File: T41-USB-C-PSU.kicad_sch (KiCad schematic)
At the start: 2 parts

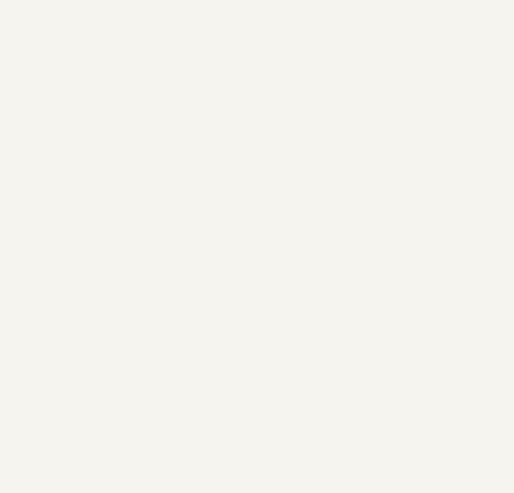
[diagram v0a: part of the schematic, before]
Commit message: Add tooling holes
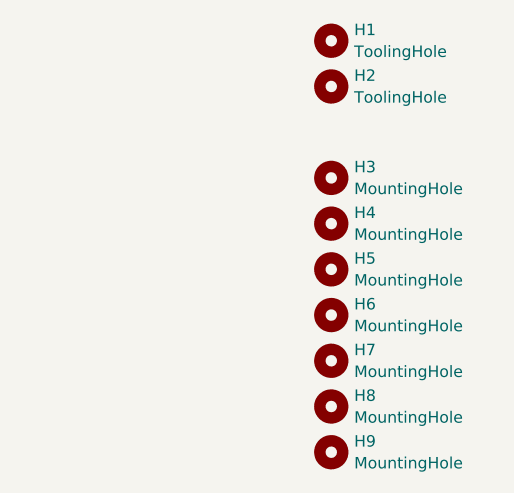
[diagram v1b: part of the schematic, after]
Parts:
- added H1, H2: ToolingHole, ToolingHole:ToolingHole_JLCSMT, symbol Mechanical:MountingHole
- added H3, H4, H5, H6, H7, H8, H9: MountingHole, MountingHole:MountingHole_2.2mm_M2, symbol Mechanical:MountingHole
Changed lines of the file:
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@@
     (stroke (width 0) (type default))
+  )
+  (symbol (lib_id "Mechanical:MountingHole") (at 267.97 35.56 0) (unit 1)
+    (in_bom no) (on_board yes) (dnp no) (fields_autoplaced)
+    (property "Reference" "H4" (at 270.51 34.3479 0)
+      (effects (font (size 1.27 1.27)) (justify left))
+    )
+    (property "Value" "MountingHole" (at 270.51 36.7721 0)
+      (effects (font (size 1.27 1.27)) (justify left))
+    )
+    (property "Footprint" "MountingHole:MountingHole_2.2mm_M2" (at 267.97 35.56 0)
+      (effects (font (size 1.27 1.27)) hide)
+    )
+    (property "Datasheet" "~" (at 267.97 35.56 0)
+      (effects (font (size 1.27 1.27)) hide)
+    )
+    (instances
+      (project "T41-USB-C-PSU"
+        (path "/4326e964-0a41-4fb3-bb68-131ba9c4f396"
+          (reference "H4") (unit 1)
+        )
+      )
+    )
+  )
+  (symbol (lib_id "Mechanical:MountingHole") (at 267.97 45.72 0) (unit 1)
+    (in_bom no) (on_board yes) (dnp no) (fields_autoplaced)
+    (property "Reference" "H6" (at 270.51 44.5079 0)
+      (effects (font (size 1.27 1.27)) (justify left))
+    )
+    (property "Value" "MountingHole" (at 270.51 46.9321 0)
+      (effects (font (size 1.27 1.27)) (justify left))
+    )
+    (property "Footprint" "MountingHole:MountingHole_2.2mm_M2" (at 267.97 45.72 0)
+      (effects (font (size 1.27 1.27)) hide)
+    )
+    (property "Datasheet" "~" (at 267.97 45.72 0)
+      (effects (font (size 1.27 1.27)) hide)
+    )
+    (instances
+      (project "T41-USB-C-PSU"
+        (path "/4326e964-0a41-4fb3-bb68-131ba9c4f396"
+          (reference "H6") (unit 1)
+        )
+      )
+    )
+  )
+  (symbol (lib_id "Mechanical:MountingHole") (at 267.97 50.8 0) (unit 1)
+    (in_bom no) (on_board yes) (dnp no) (fields_autoplaced)
+    (property "Reference" "H7" (at 270.51 49.5879 0)
+      (effects (font (size 1.27 1.27)) (justify left))
+    )
+    (property "Value" "MountingHole" (at 270.51 52.0121 0)
+      (effects (font (size 1.27 1.27)) (justify left))
+    )
+    (property "Footprint" "MountingHole:MountingHole_2.2mm_M2" (at 267.97 50.8 0)
+      (effects (font (size 1.27 1.27)) hide)
+    )
+    (property "Datasheet" "~" (at 267.97 50.8 0)
+      (effects (font (size 1.27 1.27)) hide)
+    )
+    (instances
+      (project "T41-USB-C-PSU"
+        (path "/4326e964-0a41-4fb3-bb68-131ba9c4f396"
+          (reference "H7") (unit 1)
+        )
+      )
+    )
+  )
+  (symbol (lib_id "Mechanical:MountingHole") (at 267.97 40.64 0) (unit 1)
+    (in_bom no) (on_board yes) (dnp no) (fields_autoplaced)
+    (property "Reference" "H5" (at 270.51 39.4279 0)
+      (effects (font (size 1.27 1.27)) (justify left))
+    )
+    (property "Value" "MountingHole" (at 270.51 41.8521 0)
+      (effects (font (size 1.27 1.27)) (justify left))
+    )
+    (property "Footprint" "MountingHole:MountingHole_2.2mm_M2" (at 267.97 40.64 0)
+      (effects (font (size 1.27 1.27)) hide)
+    )
+    (property "Datasheet" "~" (at 267.97 40.64 0)
+      (effects (font (size 1.27 1.27)) hide)
+    )
+    (instances
+      (project "T41-USB-C-PSU"
+        (path "/4326e964-0a41-4fb3-bb68-131ba9c4f396"
+          (reference "H5") (unit 1)
+        )
+      )
+    )
+  )
+  (symbol (lib_id "Mechanical:MountingHole") (at 267.97 15.24 0) (unit 1)
+    (in_bom no) (on_board yes) (dnp no) (fields_autoplaced)
+    (property "Reference" "H1" (at 270.51 14.0279 0)
+      (effects (font (size 1.27 1.27)) (justify left))
+    )
+    (property "Value" "ToolingHole" (at 270.51 16.4521 0)
+      (effects (font (size 1.27 1.27)) (justify left))
+    )
+    (property "Footprint" "ToolingHole:ToolingHole_JLCSMT" (at 267.97 15.24 0)
+      (effects (font (size 1.27 1.27)) hide)
+    )
+    (property "Datasheet" "~" (at 267.97 15.24 0)
+      (effects (font (size 1.27 1.27)) hide)
+    )
+    (instances
+      (project "T41-USB-C-PSU"
+        (path "/4326e964-0a41-4fb3-bb68-131ba9c4f396"
+          (reference "H1") (unit 1)
+        )
+      )
+    )
+  )
+  (symbol (lib_id "Mechanical:MountingHole") (at 267.97 60.96 0) (unit 1)
+    (in_bom no) (on_board yes) (dnp no) (fields_autoplaced)
+    (property "Reference" "H9" (at 270.51 59.7479 0)
+      (effects (font (size 1.27 1.27)) (justify left))
+    )
+    (property "Value" "MountingHole" (at 270.51 62.1721 0)
+      (effects (font (size 1.27 1.27)) (justify left))
+    )
+    (property "Footprint" "MountingHole:MountingHole_2.2mm_M2" (at 267.97 60.96 0)
+      (effects (font (size 1.27 1.27)) hide)
+    )
+    (property "Datasheet" "~" (at 267.97 60.96 0)
+      (effects (font (size 1.27 1.27)) hide)
+    )
+    (instances
+      (project "T41-USB-C-PSU"
+        (path "/4326e964-0a41-4fb3-bb68-131ba9c4f396"
+          (reference "H9") (unit 1)
+        )
+      )
+    )
+  )
+  (symbol (lib_id "Mechanical:MountingHole") (at 267.97 30.48 0) (unit 1)
+    (in_bom no) (on_board yes) (dnp no) (fields_autoplaced)
+    (property "Reference" "H3" (at 270.51 29.2679 0)
+      (effects (font (size 1.27 1.27)) (justify left))
+    )
+    (property "Value" "MountingHole" (at 270.51 31.6921 0)
+      (effects (font (size 1.27 1.27)) (justify left))
+    )
+    (property "Footprint" "MountingHole:MountingHole_2.2mm_M2" (at 267.97 30.48 0)
+      (effects (font (size 1.27 1.27)) hide)
+    )
+    (property "Datasheet" "~" (at 267.97 30.48 0)
+      (effects (font (size 1.27 1.27)) hide)
+    )
+    (instances
+      (project "T41-USB-C-PSU"
+        (path "/4326e964-0a41-4fb3-bb68-131ba9c4f396"
+          (reference "H3") (unit 1)
+        )
+      )
+    )
+  )
+  (symbol (lib_id "Mechanical:MountingHole") (at 267.97 20.32 0) (unit 1)
+    (in_bom no) (on_board yes) (dnp no) (fields_autoplaced)
+    (property "Reference" "H2" (at 270.51 19.1079 0)
+      (effects (font (size 1.27 1.27)) (justify left))
+    )
+    (property "Value" "ToolingHole" (at 270.51 21.5321 0)
+      (effects (font (size 1.27 1.27)) (justify left))
+    )
+    (property "Footprint" "ToolingHole:ToolingHole_JLCSMT" (at 267.97 20.32 0)
+      (effects (font (size 1.27 1.27)) hide)
+    )
+    (property "Datasheet" "~" (at 267.97 20.32 0)
+      (effects (font (size 1.27 1.27)) hide)
+    )
+    (instances
+      (project "T41-USB-C-PSU"
+        (path "/4326e964-0a41-4fb3-bb68-131ba9c4f396"
+          (reference "H2") (unit 1)
+        )
+      )
+    )
   )
   (symbol (lib_id "power:GND") (at 111.76 34.29 0) (unit 1)
@@
         )
       )
+    )
+  )
+  (symbol (lib_id "Mechanical:MountingHole") (at 267.97 55.88 0) (unit 1)
+    (in_bom no) (on_board yes) (dnp no) (fields_autoplaced)
+    (property "Reference" "H8" (at 270.51 54.6679 0)
+      (effects (font (size 1.27 1.27)) (justify left))
+    )
+    (property "Value" "MountingHole" (at 270.51 57.0921 0)
+      (effects (font (size 1.27 1.27)) (justify left))
+    )
+    (property "Footprint" "MountingHole:MountingHole_2.2mm_M2" (at 267.97 55.88 0)
+      (effects (font (size 1.27 1.27)) hide)
+    )
+    (property "Datasheet" "~" (at 267.97 55.88 0)
+      (effects (font (size 1.27 1.27)) hide)
+    )
+    (instances
+      (project "T41-USB-C-PSU"
+        (path "/4326e964-0a41-4fb3-bb68-131ba9c4f396"
+          (reference "H8") (unit 1)
+        )
+      )

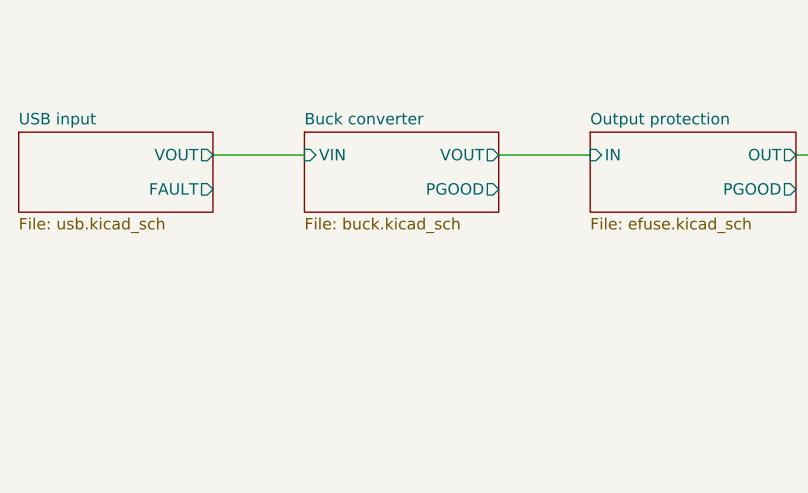
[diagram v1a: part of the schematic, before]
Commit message: Add status LEDs
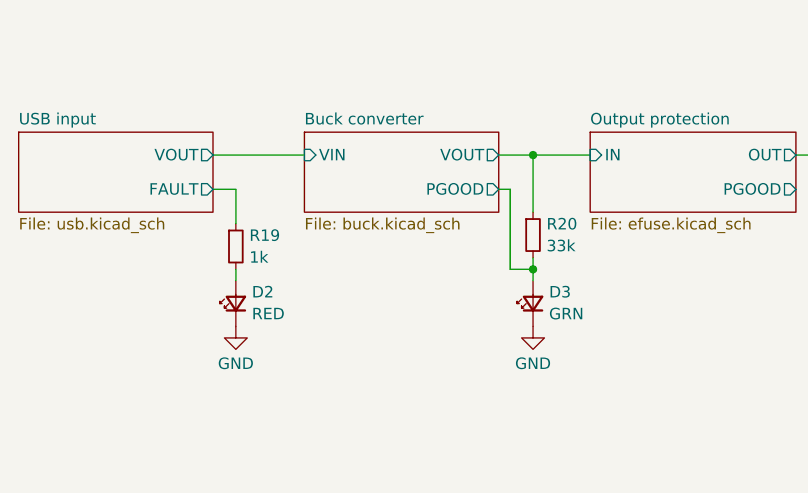
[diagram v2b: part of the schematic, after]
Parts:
- added D2: RED, LED_SMD:LED_0603_1608Metric, symbol Device:LED_Small
- added D3: GRN, LED_SMD:LED_0603_1608Metric, symbol Device:LED_Small
- added R19: 1k, Resistor_SMD:R_0402_1005Metric, symbol Device:R_Small
- added R20: 33k, Resistor_SMD:R_0402_1005Metric, symbol Device:R_Small
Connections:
- net Buck converter/PGOOD: now also D3.2 (A), R20.2
- net Buck converter/VOUT: now also R20.1
- net GND: now also D2.1 (K), D3.1 (K)
- net USB input/FAULT: now also R19.1
- new net: D2.2 (A), R19.2
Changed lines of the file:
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@@
 (kicad_sch (version 20230121) (generator eeschema)
   (paper "A4")
+  (junction (at 76.2 27.94) (diameter 0) (color 0 0 0 0)
+  )
+  (junction (at 76.2 40.64) (diameter 0) (color 0 0 0 0)
+  )
+  (wire (pts (xy 76.2 39.37) (xy 76.2 40.64))
+    (stroke (width 0) (type default))
+  )
+  (wire (pts (xy 73.66 31.75) (xy 72.39 31.75))
+    (stroke (width 0) (type default))
+  )
+  (wire (pts (xy 43.18 31.75) (xy 40.64 31.75))
+    (stroke (width 0) (type default))
+  )
+  (wire (pts (xy 76.2 40.64) (xy 76.2 41.91))
+    (stroke (width 0) (type default))
+  )
+  (wire (pts (xy 43.18 40.64) (xy 43.18 41.91))
+    (stroke (width 0) (type default))
+  )
+  (wire (pts (xy 76.2 40.64) (xy 73.66 40.64))
+    (stroke (width 0) (type default))
+  )
+  (wire (pts (xy 43.18 35.56) (xy 43.18 31.75))
+    (stroke (width 0) (type default))
+  )
   (wire (pts (xy 111.76 33.02) (xy 111.76 34.29))
     (stroke (width 0) (type default))
@@
     (stroke (width 0) (type default))
   )
-  (wire (pts (xy 72.39 27.94) (xy 82.55 27.94))
+  (wire (pts (xy 73.66 40.64) (xy 73.66 31.75))
+    (stroke (width 0) (type default))
+  )
+  (wire (pts (xy 72.39 27.94) (xy 76.2 27.94))
+    (stroke (width 0) (type default))
+  )
+  (wire (pts (xy 76.2 27.94) (xy 76.2 34.29))
     (stroke (width 0) (type default))
   )
@@
     (stroke (width 0) (type default))
   )
+  (wire (pts (xy 76.2 27.94) (xy 82.55 27.94))
+    (stroke (width 0) (type default))
+  )
+  (symbol (lib_id "Device:LED_Small") (at 76.2 44.45 90) (unit 1)
+    (in_bom yes) (on_board yes) (dnp no) (fields_autoplaced)
+    (property "Reference" "D3" (at 77.978 43.1744 90)
+      (effects (font (size 1.27 1.27)) (justify right))
+    )
+    (property "Value" "GRN" (at 77.978 45.5986 90)
+      (effects (font (size 1.27 1.27)) (justify right))
+    )
+    (property "Footprint" "LED_SMD:LED_0603_1608Metric" (at 76.2 44.45 90)
+      (effects (font (size 1.27 1.27)) hide)
+    )
+    (property "Datasheet" "~" (at 76.2 44.45 90)
+      (effects (font (size 1.27 1.27)) hide)
+    )
+    (property "LCSC" "C72043" (at 76.2 44.45 90)
+      (effects (font (size 1.27 1.27)) hide)
+    )
+    (pin "1")
+    (pin "2")
+    (instances
+      (project "T41-USB-C-PSU"
+        (path "/4326e964-0a41-4fb3-bb68-131ba9c4f396"
+          (reference "D3") (unit 1)
+        )
+      )
+    )
+  )
+  (symbol (lib_id "Device:R_Small") (at 76.2 36.83 0) (unit 1)
+    (in_bom yes) (on_board yes) (dnp no)
+    (property "Reference" "R20" (at 77.6986 35.6179 0)
+      (effects (font (size 1.27 1.27)) (justify left))
+    )
+    (property "Value" "33k" (at 77.6986 38.0421 0)
+      (effects (font (size 1.27 1.27)) (justify left))
+    )
+    (property "Footprint" "Resistor_SMD:R_0402_1005Metric" (at 76.2 36.83 0)
+      (effects (font (size 1.27 1.27)) hide)
+    )
+    (property "Datasheet" "~" (at 76.2 36.83 0)
+      (effects (font (size 1.27 1.27)) hide)
+    )
+    (property "LCSC" "C25779" (at 76.2 36.83 0)
+      (effects (font (size 1.27 1.27)) hide)
+    )
+    (pin "1")
+    (pin "2")
+    (instances
+      (project "T41-USB-C-PSU"
+        (path "/4326e964-0a41-4fb3-bb68-131ba9c4f396"
+          (reference "R20") (unit 1)
+        )
+        (path "/4326e964-0a41-4fb3-bb68-131ba9c4f396/98cf6286-8764-4ea9-aedb-123e8d8fcda0"
+          (reference "R5") (unit 1)
+        )
+        (path "/4326e964-0a41-4fb3-bb68-131ba9c4f396/6dba28e6-3589-457e-baae-b5823b45c7b3"
+          (reference "R5") (unit 1)
+        )
+      )
+    )
+  )
+  (symbol (lib_id "power:GND") (at 43.18 46.99 0) (unit 1)
+    (in_bom yes) (on_board yes) (dnp no) (fields_autoplaced)
+    (property "Reference" "#PWR017" (at 43.18 53.34 0)
+      (effects (font (size 1.27 1.27)) hide)
+    )
+    (property "Value" "GND" (at 43.18 51.1231 0)
+      (effects (font (size 1.27 1.27)))
+    )
+    (property "Footprint" "" (at 43.18 46.99 0)
+      (effects (font (size 1.27 1.27)) hide)
+    )
+    (property "Datasheet" "" (at 43.18 46.99 0)
+      (effects (font (size 1.27 1.27)) hide)
+    )
+    (pin "1")
+    (instances
+      (project "T41-USB-C-PSU"
+        (path "/4326e964-0a41-4fb3-bb68-131ba9c4f396"
+          (reference "#PWR017") (unit 1)
+        )
+      )
+    )
+  )
   (symbol (lib_id "Mechanical:MountingHole") (at 267.97 35.56 0) (unit 1)
     (in_bom no) (on_board yes) (dnp no) (fields_autoplaced)
@@
     )
   )
+  (symbol (lib_id "Device:R_Small") (at 43.18 38.1 0) (unit 1)
+    (in_bom yes) (on_board yes) (dnp no)
+    (property "Reference" "R19" (at 44.6786 36.8879 0)
+      (effects (font (size 1.27 1.27)) (justify left))
+    )
+    (property "Value" "1k" (at 44.6786 39.3121 0)
+      (effects (font (size 1.27 1.27)) (justify left))
+    )
+    (property "Footprint" "Resistor_SMD:R_0402_1005Metric" (at 43.18 38.1 0)
+      (effects (font (size 1.27 1.27)) hide)
+    )
+    (property "Datasheet" "~" (at 43.18 38.1 0)
+      (effects (font (size 1.27 1.27)) hide)
+    )
+    (property "LCSC" "C11702" (at 43.18 38.1 0)
+      (effects (font (size 1.27 1.27)) hide)
+    )
+    (pin "1")
+    (pin "2")
+    (instances
+      (project "T41-USB-C-PSU"
+        (path "/4326e964-0a41-4fb3-bb68-131ba9c4f396"
+          (reference "R19") (unit 1)
+        )
+        (path "/4326e964-0a41-4fb3-bb68-131ba9c4f396/98cf6286-8764-4ea9-aedb-123e8d8fcda0"
+          (reference "R5") (unit 1)
+        )
+        (path "/4326e964-0a41-4fb3-bb68-131ba9c4f396/6dba28e6-3589-457e-baae-b5823b45c7b3"
+          (reference "R5") (unit 1)
+        )
+      )
+    )
+  )
   (symbol (lib_id "Mechanical:MountingHole") (at 267.97 15.24 0) (unit 1)
     (in_bom no) (on_board yes) (dnp no) (fields_autoplaced)
@@
         (path "/4326e964-0a41-4fb3-bb68-131ba9c4f396"
           (reference "H1") (unit 1)
+        )
+      )
+    )
+  )
+  (symbol (lib_id "Device:LED_Small") (at 43.18 44.45 90) (unit 1)
+    (in_bom yes) (on_board yes) (dnp no) (fields_autoplaced)
+    (property "Reference" "D2" (at 44.958 43.1744 90)
+      (effects (font (size 1.27 1.27)) (justify right))
+    )
+    (property "Value" "RED" (at 44.958 45.5986 90)
+      (effects (font (size 1.27 1.27)) (justify right))
+    )
+    (property "Footprint" "LED_SMD:LED_0603_1608Metric" (at 43.18 44.45 90)
+      (effects (font (size 1.27 1.27)) hide)
+    )
+    (property "Datasheet" "~" (at 43.18 44.45 90)
+      (effects (font (size 1.27 1.27)) hide)
+    )
+    (property "LCSC" "C2286" (at 43.18 44.45 90)
+      (effects (font (size 1.27 1.27)) hide)
+    )
+    (pin "1")
+    (pin "2")
+    (instances
+      (project "T41-USB-C-PSU"
+        (path "/4326e964-0a41-4fb3-bb68-131ba9c4f396"
+          (reference "D2") (unit 1)
         )
       )
@@
         )
       )
+    )
+  )
+  (symbol (lib_id "power:GND") (at 76.2 46.99 0) (unit 1)
+    (in_bom yes) (on_board yes) (dnp no) (fields_autoplaced)
+    (property "Reference" "#PWR027" (at 76.2 53.34 0)
+      (effects (font (size 1.27 1.27)) hide)
+    )
+    (property "Value" "GND" (at 76.2 51.1231 0)
+      (effects (font (size 1.27 1.27)))
+    )
+    (property "Footprint" "" (at 76.2 46.99 0)
+      (effects (font (size 1.27 1.27)) hide)
+    )
+    (property "Datasheet" "" (at 76.2 46.99 0)
+      (effects (font (size 1.27 1.27)) hide)
+    )
+    (pin "1")
+    (instances
+      (project "T41-USB-C-PSU"
+        (path "/4326e964-0a41-4fb3-bb68-131ba9c4f396"
+          (reference "#PWR027") (unit 1)
+        )
+      )

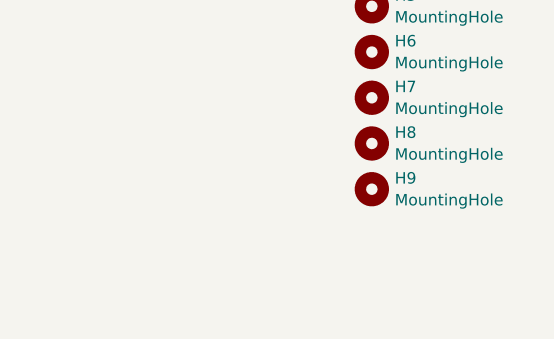
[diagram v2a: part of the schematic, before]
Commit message: Add generic case footprint
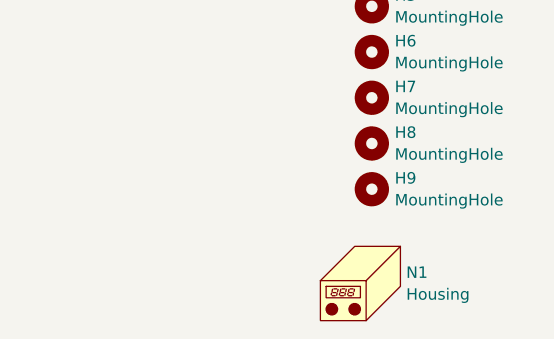
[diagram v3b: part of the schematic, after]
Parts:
- added N1: Housing, Case:Generic_Case, symbol Mechanical:Housing
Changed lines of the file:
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@@
+    )
+  )
+  (symbol (lib_id "Mechanical:Housing") (at 267.97 71.12 0) (unit 1)
+    (in_bom yes) (on_board yes) (dnp no) (fields_autoplaced)
+    (property "Reference" "N1" (at 271.78 70.2254 0)
+      (effects (font (size 1.27 1.27)) (justify left))
+    )
+    (property "Value" "Housing" (at 271.78 72.6496 0)
+      (effects (font (size 1.27 1.27)) (justify left))
+    )
+    (property "Footprint" "Case:Generic_Case" (at 269.24 69.85 0)
+      (effects (font (size 1.27 1.27)) hide)
+    )
+    (property "Datasheet" "~" (at 269.24 69.85 0)
+      (effects (font (size 1.27 1.27)) hide)
+    )
+    (instances
+      (project "T41-USB-C-PSU"
+        (path "/4326e964-0a41-4fb3-bb68-131ba9c4f396"
+          (reference "N1") (unit 1)
+        )
+      )
     )
   )
